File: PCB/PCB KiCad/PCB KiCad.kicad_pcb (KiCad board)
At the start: 2 copper layers, 40 x 40 mm, 54 parts, among them J1 Conn_01x04, J2 Qwiic, J3 Conn_01x04, J4 Conn_01x04, J5 Conn_01x04, U1 OPA2376AID, U2 NAU7802SGI, U3 TLC59208FIPWR, U4 LP5951MFX-1.8_NOPB

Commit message: Minor schematic cleanup!
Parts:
- removed the C14 at (68.8, 131.3)
- removed the D10 at (75.4, 129.3)
- removed H1, H2, H4: MountingHole, MountingHole:MountingHole_3.2mm_M3
- removed the J4 at (62.2, 140.5)
- removed the R11 at (93.9, 142.0)
- removed the R15 at (66.0, 130.4)
- added ?: MountingHole_3.2mm_M3, MountingHole:MountingHole_3.2mm_M3, F.Cu at (119.0, 32.0)
- added ?: MountingHole_3.2mm_M3, MountingHole:MountingHole_3.2mm_M3, F.Cu at (47.0, 144.0)
- added A1: Arduino_UNO_R3, Module:Arduino_UNO_R3, F.Cu at (73.7, 42.1)
- added C15: 22u, Capacitor_SMD:C_0805_2012Metric_Pad1.18x1.45mm_HandSolder, F.Cu at (59.2, 110.7)
- added C16: 100n, Capacitor_SMD:C_0805_2012Metric_Pad1.18x1.45mm_HandSolder, F.Cu at (109.8, 130.5)
- added D11: 1720nm, LED_SMD:LED_1206_3216Metric_Pad1.42x1.75mm_HandSolder, F.Cu at (78.4, 131.0)
- added D12: LED RED, LED_SMD:LED_0805_2012Metric_Pad1.15x1.40mm_HandSolder, F.Cu at (53.6, 103.6)
- added D3: LED RED, LED_SMD:LED_0805_2012Metric_Pad1.15x1.40mm_HandSolder, F.Cu at (91.4, 33.4)
- added G***: LOGO, LOGO, F.Cu at (118.9, 48.5)
- added G***: LOGO, LOGO, F.Cu at (118.6, 40.5)
- added G***: LOGO, LOGO, B.Cu at (83.4, 121.0)
- added G1: LOGO, LOGO, B.Cu at (82.0, 66.0)
- added J2: Conn_01x08, Connector_PinHeader_2.54mm:PinHeader_1x08_P2.54mm_Vertical, F.Cu at (47.3, 119.2)
- added R16: 47, Resistor_SMD:R_0805_2012Metric_Pad1.20x1.40mm_HandSolder, F.Cu at (96.8, 137.3)
- added R17: 47, Resistor_SMD:R_0805_2012Metric_Pad1.20x1.40mm_HandSolder, F.Cu at (96.8, 139.8)
- added R18: 47, Resistor_SMD:R_0805_2012Metric_Pad1.20x1.40mm_HandSolder, F.Cu at (96.8, 142.4)
- added R19: 47, Resistor_SMD:R_0805_2012Metric_Pad1.20x1.40mm_HandSolder, F.Cu at (69.7, 142.2)
- added R20: 47, Resistor_SMD:R_0805_2012Metric_Pad1.20x1.40mm_HandSolder, F.Cu at (69.7, 139.8)
- added R21: 47, Resistor_SMD:R_0805_2012Metric_Pad1.20x1.40mm_HandSolder, F.Cu at (69.7, 137.3)
- added R22: 47, Resistor_SMD:R_0805_2012Metric_Pad1.20x1.40mm_HandSolder, F.Cu at (69.7, 134.5)
- added R7: 100, Resistor_SMD:R_0805_2012Metric_Pad1.20x1.40mm_HandSolder, F.Cu at (88.2, 33.4)
- added R8: 100, Resistor_SMD:R_0805_2012Metric_Pad1.20x1.40mm_HandSolder, F.Cu at (94.7, 33.4)
- added REF**: MountingHole_3.2mm_M3, MountingHole:MountingHole_3.2mm_M3, F.Cu at (47.0, 32.0)
- added SW1: MCU_RESET, Button_Switch_THT:SW_PUSH_6mm, F.Cu at (63.7, 31.7)
- added SW2: TRIGGER, Button_Switch_THT:SW_PUSH_6mm, F.Cu at (53.5, 31.8)
- added e: MountingHole_3.2mm_M3, MountingHole:MountingHole_3.2mm_M3, F.Cu at (47.0, 102.0)
- added e: MountingHole_3.2mm_M3, MountingHole:MountingHole_3.2mm_M3, F.Cu at (119.0, 144.0)
- added e: MountingHole_3.2mm_M3, MountingHole:MountingHole_3.2mm_M3, F.Cu at (119.0, 102.0)
- C1, C10, C11, C2, C3, C4, C5, C6, C7, C8, C9, FB1, R1, R2, R3, R4, R5, R6, U1, U2: moved to F.Cu
- C13: value 22u -> 10u; moved to F.Cu
- C14: renamed from C12; moved to F.Cu
- D1: footprint Diode_THT:D_A-405_P2.54mm_Vertical_KathodeUp -> Diode_SMD:D_1206_3216Metric_Pad1.42x1.75mm_HandSolder
- D2: value LED RED -> LED BLUE; moved to F.Cu
- G***: moved to B.Cu
- J3: renamed from J2; moved to F.Cu
- R10, R9: value 47 -> 10k
- R11: renamed from R7; moved to F.Cu
- R12, R13: value 47 -> 4.7k
- R14: value 47 -> 1k
- U3: value TLC59208FIPWR -> AMS1117-3.3; footprint TLC59208:Texas_Instruments-TLC59208FIPWR-Level_A -> Package_TO_SOT_SMD:SOT-223-3_TabPin2; moved to F.Cu
- U4: value LP5951MFX-1.8_NOPB -> TLC59208FIPWR; footprint LP5951MFX-1.8_NOPB:SOT95P280X145-5N -> TLC59208:Texas_Instruments-TLC59208FIPWR-Level_A; moved to F.Cu
- moved D2 119.0 mm to (84.9, 33.4)
- moved R10 106.5 mm to (74.7, 33.4), turned to -90 degrees
- moved R9 102.2 mm to (77.5, 33.4), turned to -90 degrees
- moved C10 64.2 mm to (113.8, 108.4)
- moved R12 60.2 mm to (118.8, 112.9), turned to 180 degrees
- moved R13 57.6 mm to (118.8, 114.9), turned to 180 degrees
- moved R11 55.6 mm to (53.6, 100.0), turned to 180 degrees
- moved G*** 52.4 mm to (98.1, 104.1), turned to 180 degrees
- moved C13 47.4 mm to (64.9, 104.8)
- moved G*** 47.2 mm to (106.4, 104.3)
- moved R5 46.8 mm to (111.1, 101.2), turned to 90 degrees
- moved U2 44.2 mm to (111.5, 116.6), turned to 0 degrees
- moved R6 44.2 mm to (109.0, 101.2), turned to 90 degrees
- moved R14 43.8 mm to (109.8, 132.7)
- moved C14 43.8 mm to (56.7, 110.7), turned to 90 degrees
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- renumbered D9 to D10, D3 to D4, D4 to D5, D5 to D6, D6 to D7, D7 to D8, D8 to D9, J3 to J4, R8 to R15
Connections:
- C1 pad 2: 3.3v -> +3.3V
- C10 pad 1: 3.3v -> +3.3V
- C13 pad 1: 3.3v -> 5v_RAW
- C14 pad 2: 3.3v -> +3.3V
- D10 pad 1: Net-(D9-K) -> Net-(D10-K)
- D10 pad 2: 3.3v -> +3.3V
- D4 pad 2: 3.3v -> +3.3V
- D5 pad 1: Net-(D4-K) (its old number) -> Net-(D5-K)
- D5 pad 2: 3.3v -> +3.3V
- D6 pad 1: Net-(D5-K) -> Net-(D6-K)
- D6 pad 2: 3.3v -> +3.3V
- D7 pad 2: 3.3v -> +3.3V
- D8 pad 1: Net-(D7-K) (its old number) -> Net-(D8-K)
- D8 pad 2: 3.3v -> +3.3V
- D9 pad 1: Net-(D8-K) -> Net-(D9-K)
- D9 pad 2: 3.3v -> +3.3V
- FB1 pad 1: 3.3v -> +3.3V
- J1 pad 1: 3.3v -> +3.3V
- R10 pad 1: LED3 -> 5v_RAW
- R10 pad 2: Net-(D5-K) -> TRIGGER
- R11 pad 1: 3.3v -> 3v3unf
- R11 pad 2: Net-(D2-A) -> Net-(D12-A)
- R12 pad 1: LED5 -> +3.3V
- R12 pad 2: Net-(D7-K) (its old number) -> SDA
- R13 pad 1: LED6 -> +3.3V
- R13 pad 2: Net-(D8-K) -> SCL
- R14 pad 1: LED7 -> LED_RESET
- R14 pad 2: Net-(D9-K) -> +3.3V
- R6 pad 2: Net-(U4-VOUT) -> +3.3V
- R9 pad 1: LED2 -> 5v_RAW
- R9 pad 2: Net-(D4-K) (its old number) -> MCU_RESET
- U1 pad 3: 3.3v -> +3.3V
- U1 pad 5: 3.3v -> +3.3V
- U1 pad 8: 3.3v -> +3.3V
- U2 pad 12: unconnected-(U2-DRDY-Pad12) -> DRDY_INT
- U2 pad 15: 3.3v -> +3.3V
- U2 pad 16: 3.3v -> +3.3V
- U3 pad 2: GND -> 3v3unf
- U3 pad 3: GND -> 5v_RAW
- U4 pad 1: 3.3v -> GND
- U4 pad 3: 3.3v -> GND
- U4 pad 4: (no net) -> LED1
- U4 pad 5: Net-(U4-VOUT) -> LED2
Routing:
- net +3.3V: track 0.00 -> 200.4 mm, vias 0 -> 4
- net TRIGGER: track 0.00 -> 181.0 mm, vias 0 -> 1
- net DRDY_INT: track 0.00 -> 159.9 mm, vias 0 -> 1
- net LED_RESET: track 0.00 -> 159.8 mm, vias 0 -> 1
- net 3.3v: track 156.1 -> 0.00 mm
- net 5v_RAW: track 0.00 -> 155.9 mm, vias 0 -> 2
- net SCL: track 27.6 -> 160.7 mm, vias 0 -> 1
- net SDA: track 39.7 -> 151.7 mm, vias 0 -> 1
- net LED_BLUE: track 0.00 -> 60.5 mm, vias 0 -> 1
- net LED6: track 9.73 -> 57.8 mm, vias 0 -> 1
- net LED7: track 10.9 -> 58.2 mm, vias 0 -> 1
- net LED8: track 12.2 -> 58.6 mm, vias 0 -> 1
- net LED5: track 10.7 -> 56.9 mm, vias 0 -> 1
- net 3v3unf: track 5.64 -> 40.9 mm
- net MCU_RESET: track 0.00 -> 22.3 mm
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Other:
- board size 40 x 40 mm -> 80.1 x 120 mm
- board text added: "Act"
- board text added: "GND 3.3V SDA SCL LED RST DRDY TRIG 5V raw"
- board text added: "Plastic Scanner Development Board 2.3 May 2023"
- board text added: "Plastic Scanner Development Board 2.3.1A 2025-03-03"
- board text added: "Power"
- board text added: "Reset"
- board text added: "S/N"
- board text added: "Trigger"
- board text removed: "Plastic Scanner Development Board 2.4 November 2023"

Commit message: Giant schematic cleanup to make more sense of the sensor circuit and just clean everything up a bit.
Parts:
- U1: value OPA2376AID -> OPA2376xxD
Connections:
- net /ADC/AIN+ renamed AIN+
- net /ADC/AIN- renamed AIN-
- net /Sensor/A+ renamed A+
- net /Sensor/A- renamed A-
- net 5v_RAW renamed +5V
- net LED1 renamed /LED/LED1
- net LED2 renamed /LED/LED2
- net LED3 renamed /LED/LED3
- net LED4 renamed /LED/LED4
- net LED5 renamed /LED/LED5
- net LED6 renamed /LED/LED6
- net LED7 renamed /LED/LED7
- net LED8 renamed /LED/LED8
- net LED_BLUE renamed /MCU + IO/LED_BLUE
- net MCU_RESET renamed /MCU + IO/NRESET

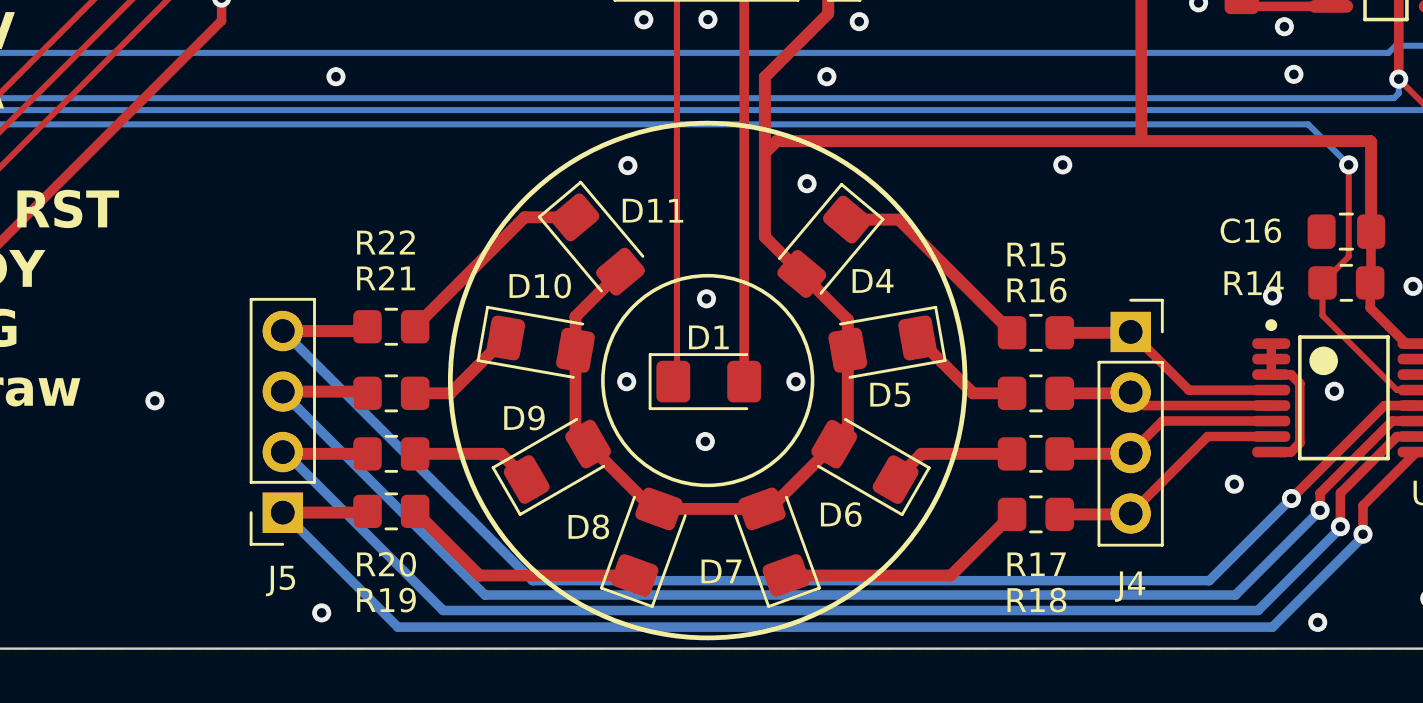
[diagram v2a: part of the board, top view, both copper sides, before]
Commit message: Relabel LEDs 0 - 7 and put that on the silkscreen for reference.
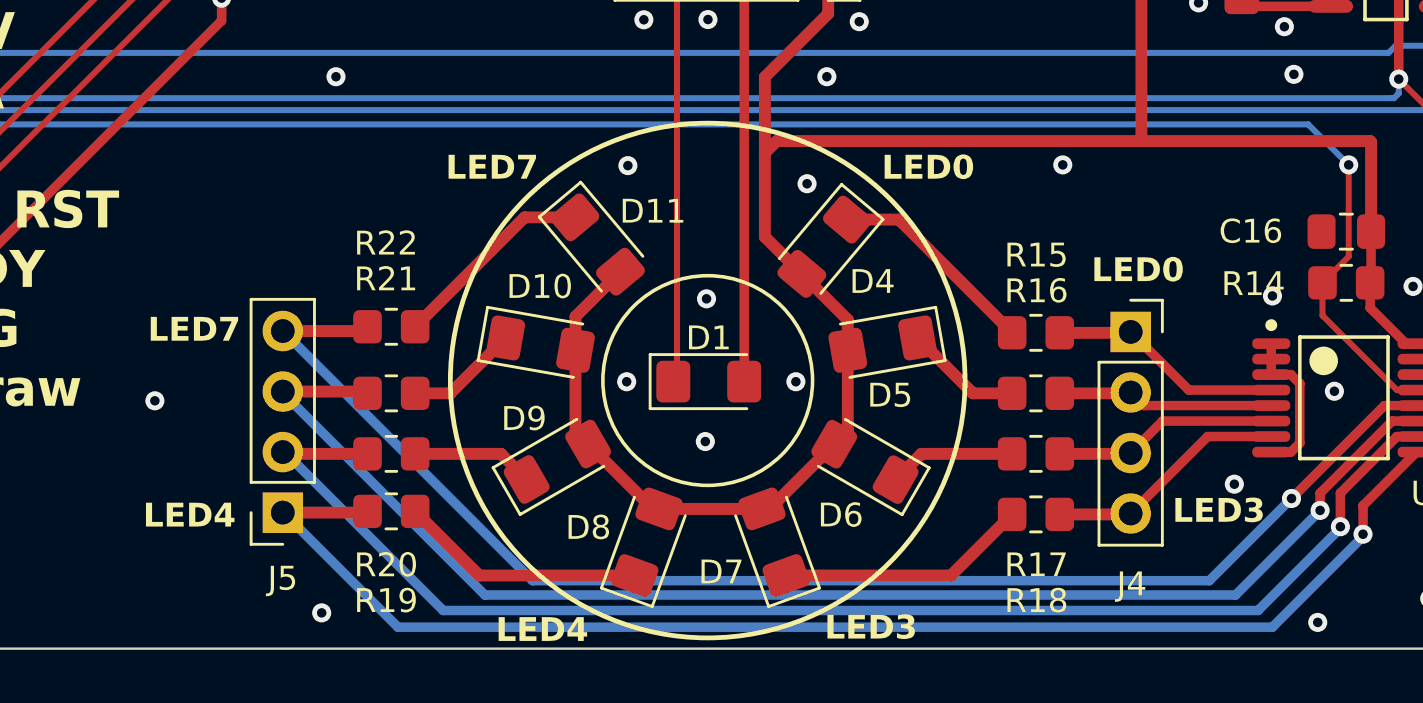
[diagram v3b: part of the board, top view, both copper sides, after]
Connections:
- J4 pad 1: /LED/LED1 -> /LED/LED0
- J4 pad 2: /LED/LED2 -> /LED/LED1
- J4 pad 3: /LED/LED3 -> /LED/LED2
- J4 pad 4: /LED/LED4 -> /LED/LED3
- J5 pad 1: /LED/LED5 -> /LED/LED4
- J5 pad 2: /LED/LED6 -> /LED/LED5
- J5 pad 3: /LED/LED7 -> /LED/LED6
- J5 pad 4: /LED/LED8 -> /LED/LED7
- R15 pad 1: /LED/LED1 -> /LED/LED0
- R16 pad 1: /LED/LED2 -> /LED/LED1
- R17 pad 1: /LED/LED3 -> /LED/LED2
- R18 pad 1: /LED/LED4 -> /LED/LED3
- R19 pad 1: /LED/LED5 -> /LED/LED4
- R20 pad 1: /LED/LED6 -> /LED/LED5
- R21 pad 1: /LED/LED7 -> /LED/LED6
- R22 pad 1: /LED/LED8 -> /LED/LED7
- U4 pad 10: /LED/LED6 -> /LED/LED5
- U4 pad 11: /LED/LED7 -> /LED/LED6
- U4 pad 12: /LED/LED8 -> /LED/LED7
- U4 pad 4: /LED/LED1 -> /LED/LED0
- U4 pad 5: /LED/LED2 -> /LED/LED1
- U4 pad 6: /LED/LED3 -> /LED/LED2
- U4 pad 7: /LED/LED4 -> /LED/LED3
- U4 pad 9: /LED/LED5 -> /LED/LED4
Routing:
- net /LED/LED8: track 58.6 -> 0.00 mm, vias 1 -> 0
- net /LED/LED4: track 10.2 -> 56.9 mm, vias 0 -> 1
- net /LED/LED0: track 0.00 -> 9.90 mm
- net /LED/LED5: track 56.9 -> 57.8 mm
- net /LED/LED3: track 9.45 -> 10.2 mm
- net /LED/LED1: track 9.90 -> 9.12 mm
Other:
- board text added: "LED0"
- board text added: "LED3"
- board text added: "LED4"
- board text added: "LED7"
